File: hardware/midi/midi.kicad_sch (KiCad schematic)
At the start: 49 parts, among them J2 Midi Out, J4 Power, J6 MIDI In, J7 USB_A, J8 I2C0, J9 I2C1, Q1 BSS138, Q3 TSM680P06, Q4 BSS138, SW1 Reset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

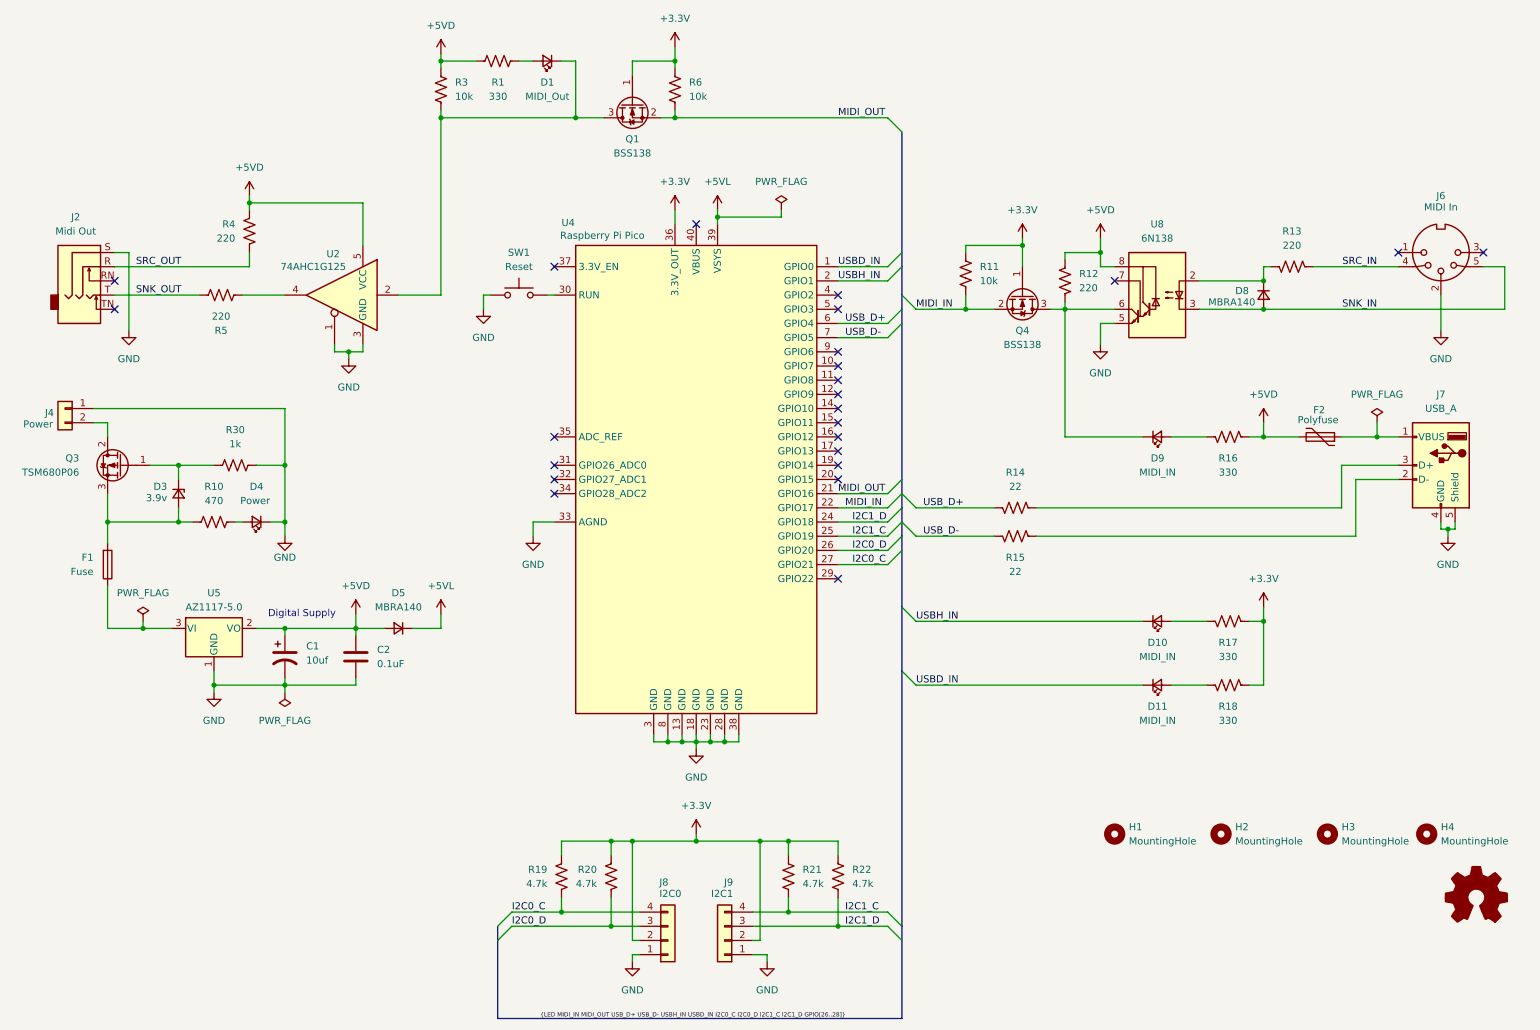
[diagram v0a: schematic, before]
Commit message: Rev 1.1: - Update to latest KiCad - Fixed short in servo board - Updates to right-angle diag connector on servo boards - Fixed microproc footprint on diag board - Flipped I2C connector to top of diag board - Pass all ERC and DRC checks, add exclusions
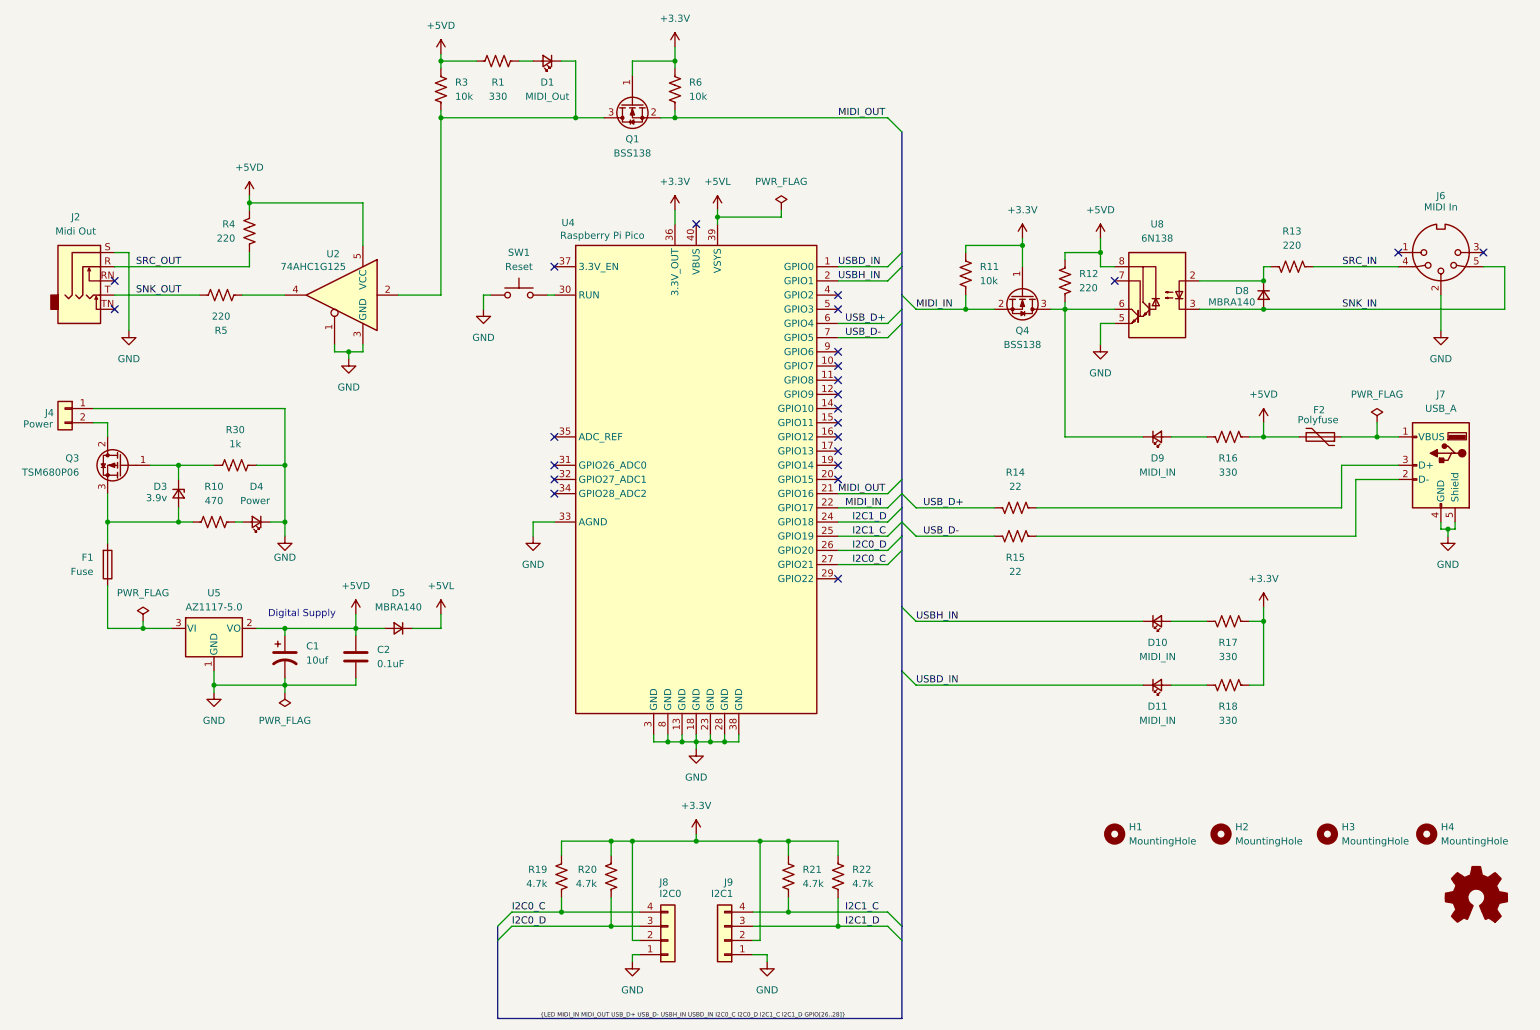
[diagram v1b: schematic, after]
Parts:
- Q3: symbol Device:Q_PMOS_GDS -> Transistor_FET:Q_PMOS_GDS
- U4: footprint footprints:RP_Pico_DIP -> Package_DIP:DIP-40_W15.24mm
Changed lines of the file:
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@@
 (kicad_sch
-	(version 20231120)
+	(version 20250114)
 	(generator "eeschema")
-	(generator_version "8.0")
+	(generator_version "9.0")
 	(paper "A4")
 	(title_block
 		(title "Animatronics - MIDI (ANI-MID)")
-		(date "2025-02-09")
-		(rev "1.0")
+		(date "2025-12-31")
+		(rev "1.1")
 		(company "Sparky Bobo Designs")
 		(comment 2 "Designed by: SparkyBobo")
@@
 		(comment 4 "Released under the Creative Commons Attribution Share-Alike 4.0 License")
 	)
+	(text "Digital Supply"
+		(exclude_from_sim no)
+		(at 66.548 123.19 0)
+		(effects
+			(font
+				(size 1.27 1.27)
+			)
+		)
+	)
 	(junction
 		(at 125.73 163.83)
@@
 		)
 	)
-	(text "Digital Supply"
-		(exclude_from_sim no)
-		(at 66.548 123.19 0)
-		(effects
-			(font
-				(size 1.27 1.27)
-			)
-		)
-	)
 	(label "USBH_IN"
 		(at 162.56 63.5 0)
@@
 	)
 	(symbol
-		(lib_id "Device:Q_PMOS_GDS")
+		(lib_id "Transistor_FET:Q_PMOS_GDS")
 		(at 34.29 96.52 0)
 		(mirror y)
@@
 			)
 		)
-		(property "Datasheet" "https://www.adafruit.com/product/1699"
+		(property "Datasheet" "~"
 			(at 27.94 60.96 0)
 			(effects
@@
 			)
 		)
+		(property "Sim.Pin" "1=K 2=A"
+			(at 110.49 24.13 0)
+			(effects
+				(font
+					(size 1.27 1.27)
+				)
+				(hide yes)
+			)
+		)
 		(pin "2"
 		)
@@
 			)
 		)
+		(property "Sim.Pin" "1=K 2=A"
+			(at 219.71 124.46 0)
+			(effects
+				(font
+					(size 1.27 1.27)
+				)
+				(hide yes)
+			)
+		)
 		(pin "2"
 		)
@@
 			)
 		)
+		(property "Sim.Pin" "1=K 2=A"
+			(at 219.71 91.44 0)
+			(effects
+				(font
+					(size 1.27 1.27)
+				)
+				(hide yes)
+			)
+		)
 		(pin "2"
 		)
@@
 			)
 		)
-		(property "Footprint" "footprints:RP_Pico_DIP"
+		(property "Footprint" "Package_DIP:DIP-40_W15.24mm"
 			(at 137.16 99.06 0)
 			(effects
@@
 			)
 		)
+		(property "Sim.Pin" "1=K 2=A"
+			(at 58.42 106.68 0)
+			(effects
+				(font
+					(size 1.27 1.27)
+				)
+				(hide yes)
+			)
+		)
 		(pin "2"
 		)
@@
 			)
 		)
+		(property "Sim.Pin" "1=K 2=A"
+			(at 219.71 135.89 0)
+			(effects
+				(font
+					(size 1.27 1.27)
+				)
+				(hide yes)
+			)
+		)
 		(pin "2"
 		)
@@
 			)
 		)
-		(property "Datasheet" "https://www.adafruit.com/product/367"
+		(property "Datasheet" "~"
 			(at 105.41 60.96 0)
 			(effects
@@
 		)
 	)
+	(embedded_fonts no)
 )
